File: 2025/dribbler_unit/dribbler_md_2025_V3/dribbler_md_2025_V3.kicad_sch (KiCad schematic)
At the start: 114 parts, among them J2 Conn_01x04_Pin, J3 Conn_01x02_Pin, J4 Conn_01x07_Pin, J5 Conn_01x03_Pin, J6 Conn_01x02_Pin, J7 Conn_01x02_Pin, J8 Conn_01x02_Socket, SW2 SW_MEC_5E, SW4 SW_MEC_5E, U1 MAX3051, U2 STS8DN3LLH5, U3 STS8DN3LLH5, U4 DRV8701, U5 STM32F446RETx, Y1 Crystal_GND2

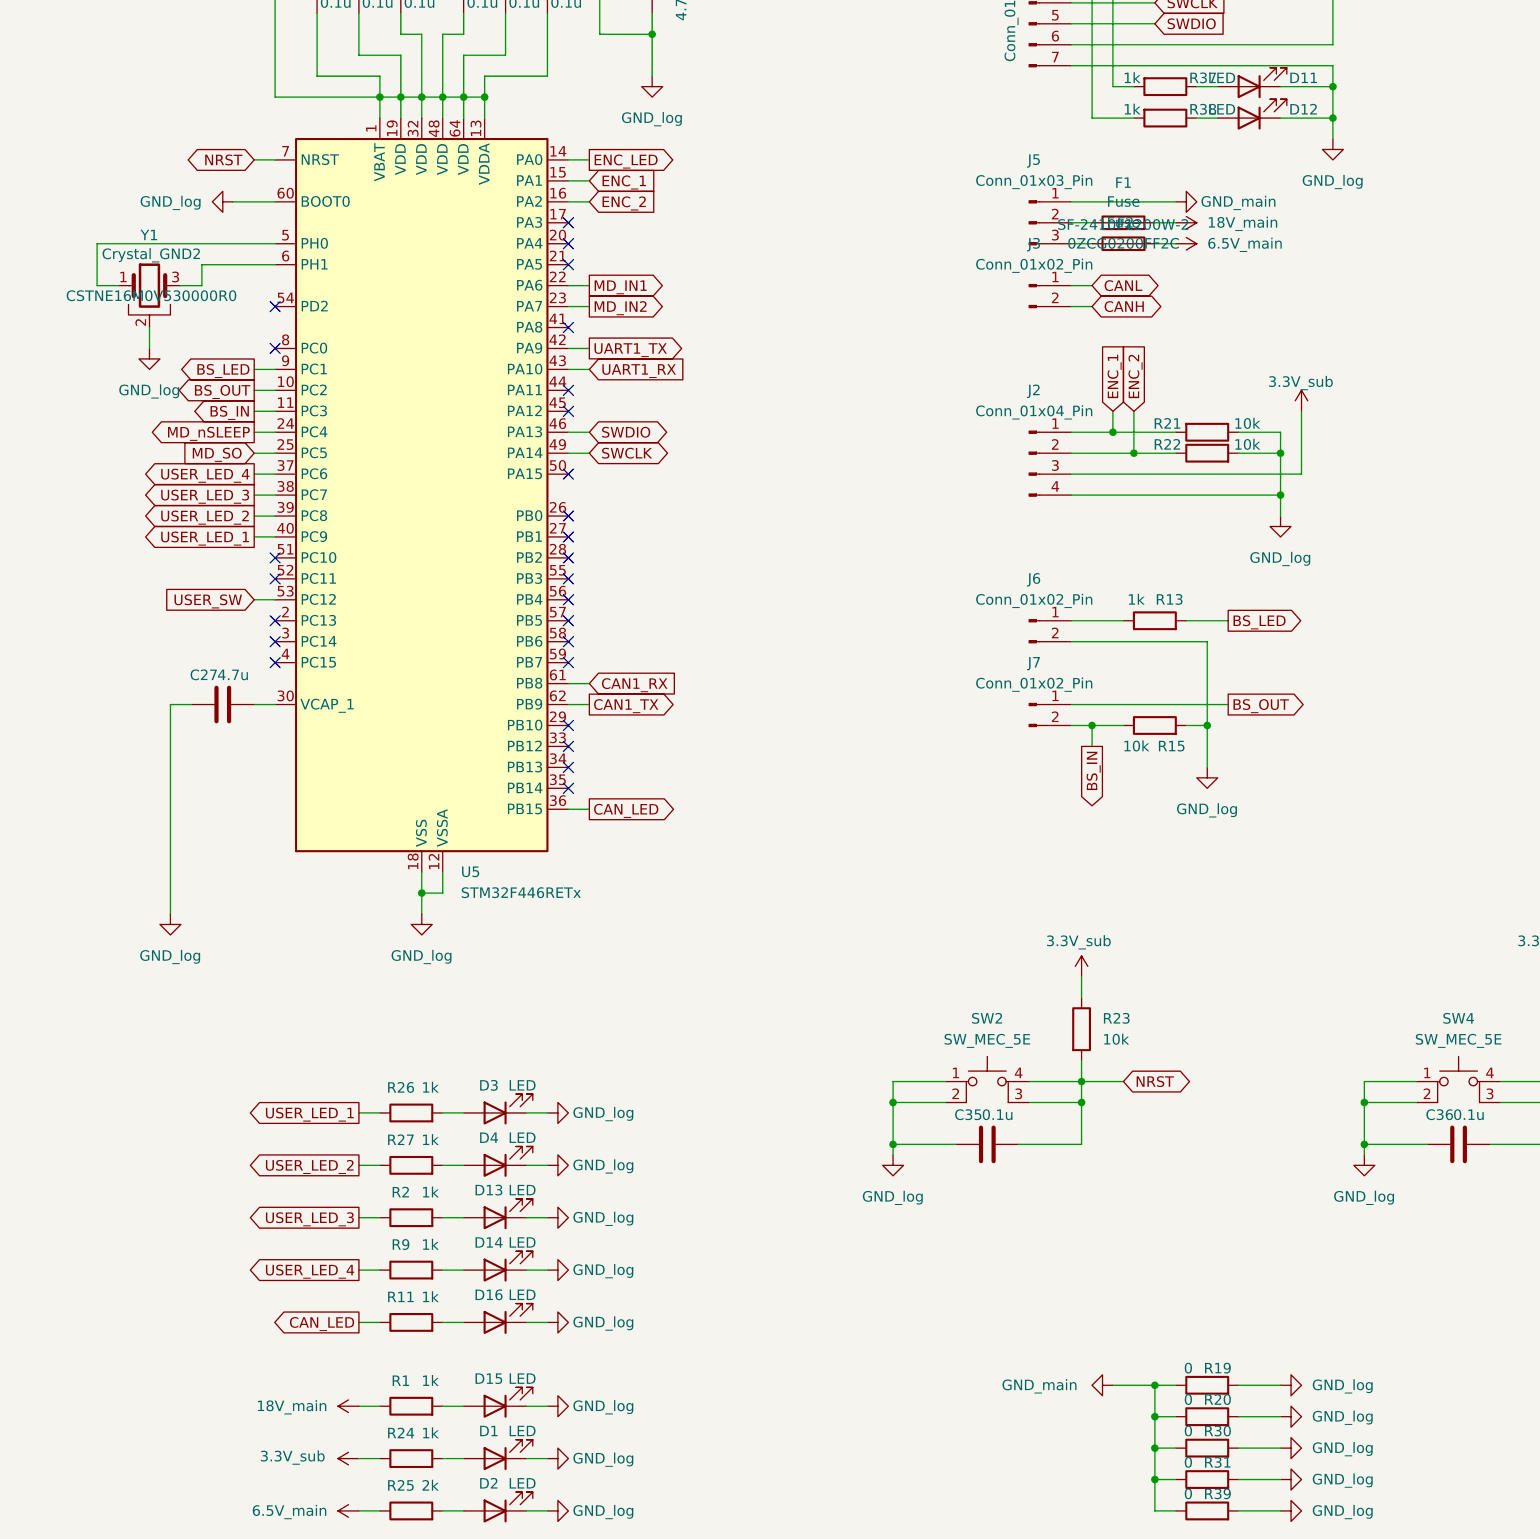
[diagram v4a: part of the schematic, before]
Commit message: stm周りを配線
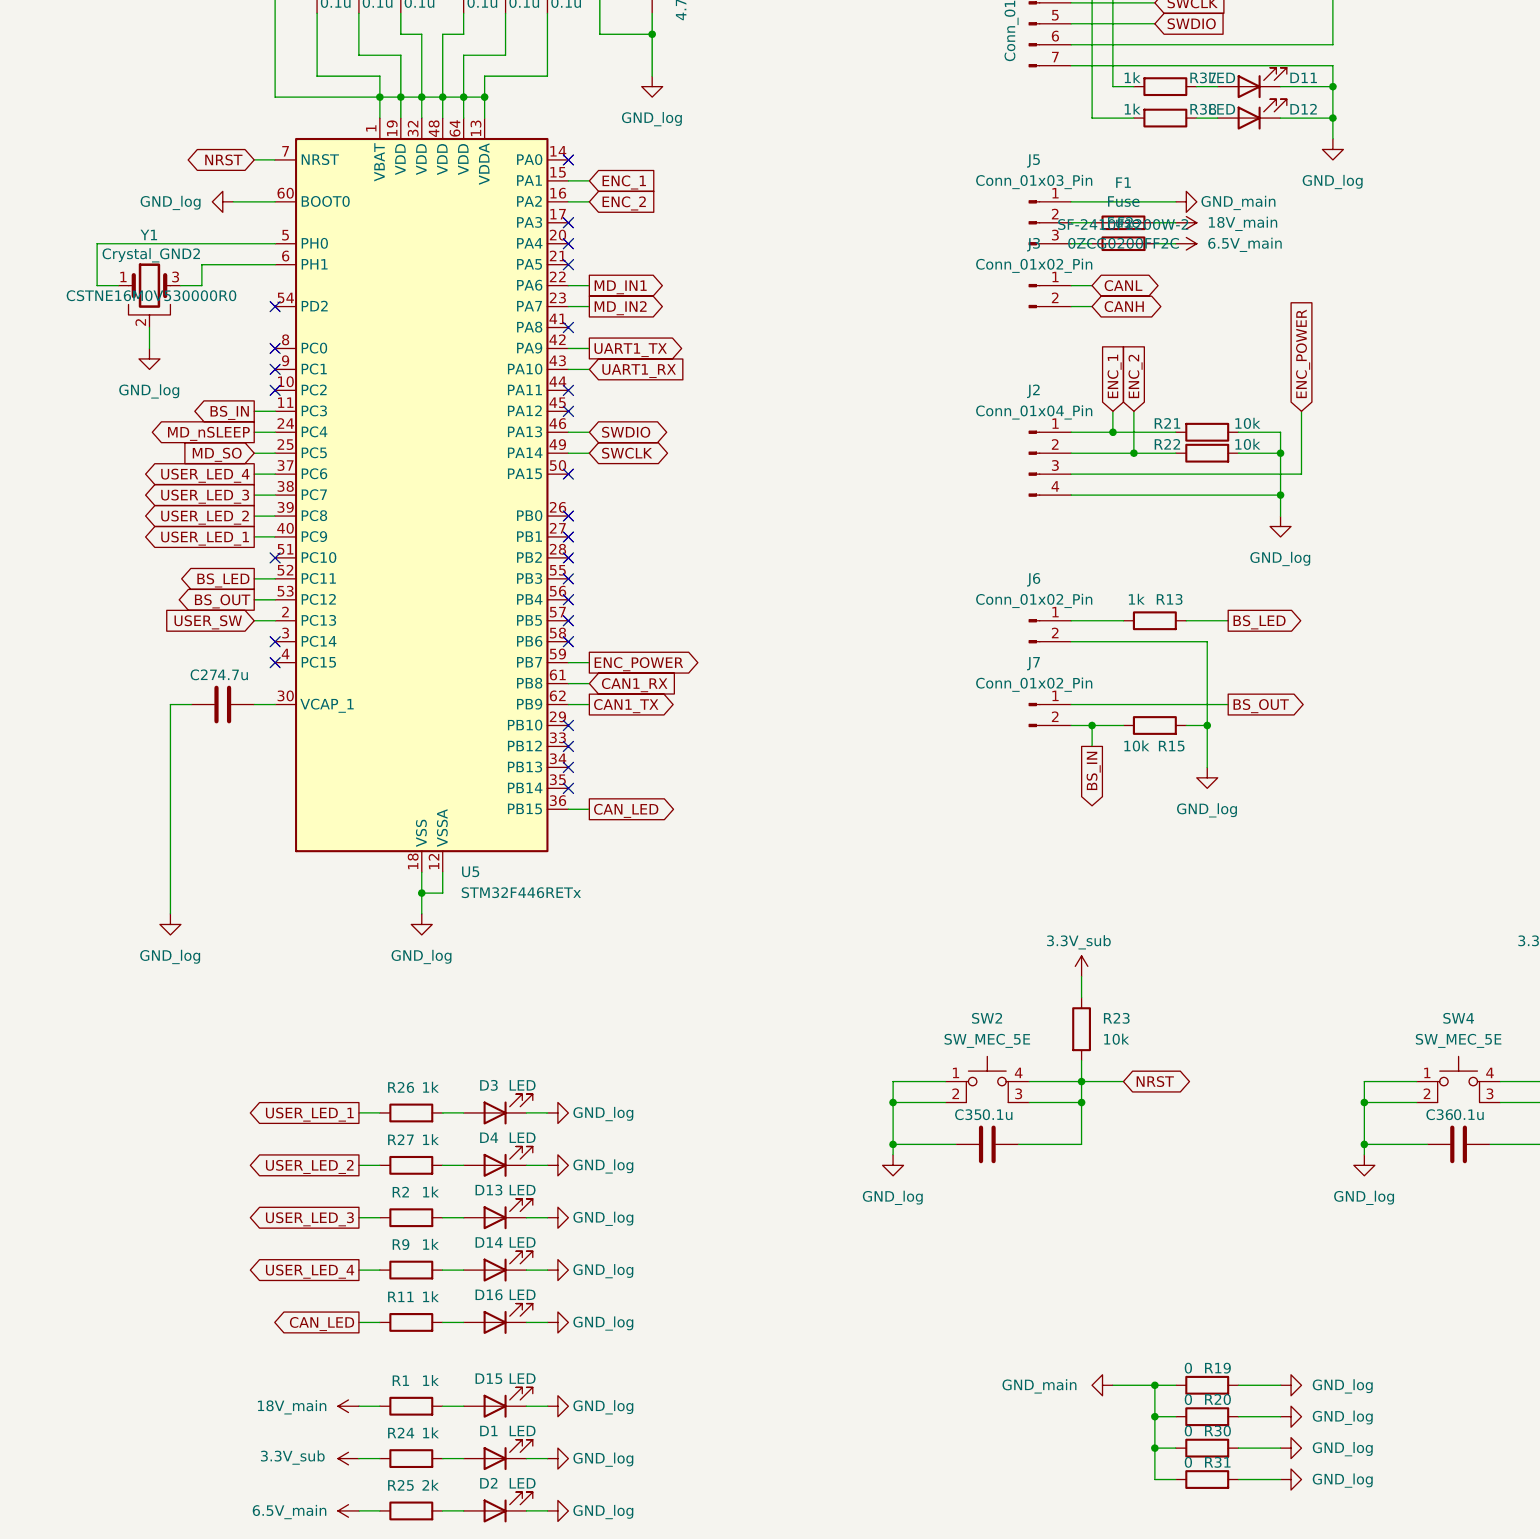
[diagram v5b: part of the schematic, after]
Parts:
- removed R39: 0, Resistor_SMD:R_0603_1608Metric_Pad0.98x0.95mm_HandSolder, symbol Device:R
- R11, R2, R26, R27, R9: footprint Resistor_SMD:R_0603_1608Metric_Pad0.98x0.95mm_HandSolder -> Resistor_SMD:R_0402_1005Metric_Pad0.72x0.64mm_HandSolder
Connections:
- net 3.3V_sub: no longer J2.3 (Pin_3)
- net BS_LED: now also U5.52 (PC11); no longer U5.9 (PC1)
- net BS_OUT: now also U5.53 (PC12); no longer U5.10 (PC2)
- net USER_SW: now also U5.2 (PC13); no longer U5.53 (PC12)
- net ENC_POWER: now reaches U5.59 (PB7)
- net ENC_POWER: now also J2.3 (Pin_3)
- net ENC_LED: no longer names the net of U5.14 (PA0)

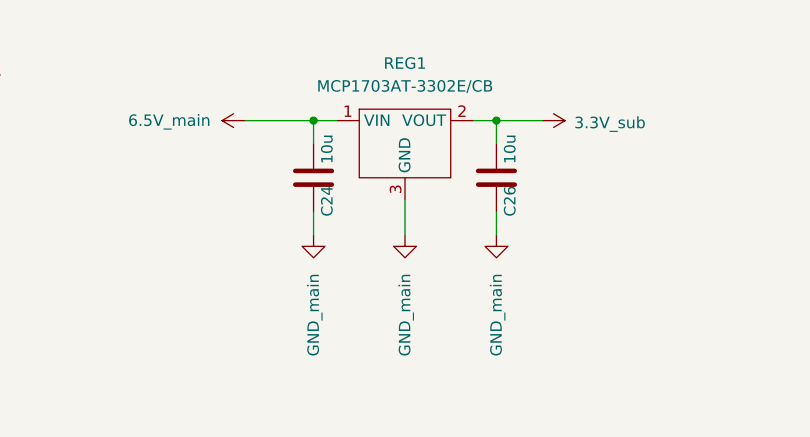
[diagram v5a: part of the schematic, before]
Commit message: 配線完了（ビア打ちは未完了）
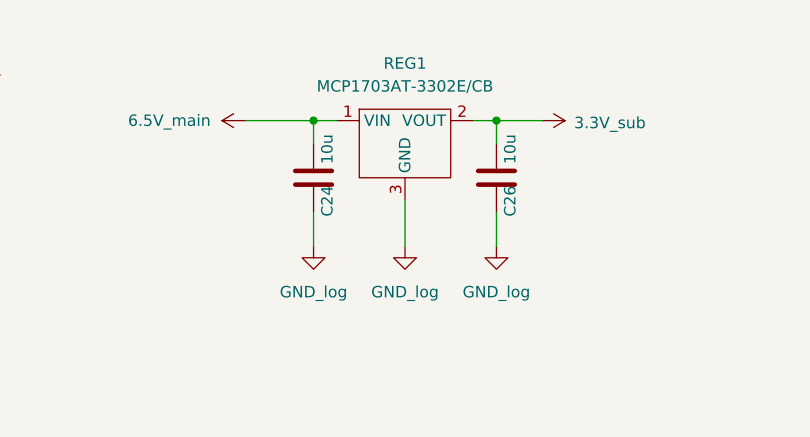
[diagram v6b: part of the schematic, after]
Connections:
- net GND_log: now also C24.2, C26.2, REG1.3 (GND)
- net GND_main: no longer C24.2, C26.2, REG1.3 (GND)
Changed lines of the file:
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@@
 	(wire
 		(pts
-			(xy 149.86 201.93) (xy 149.86 204.47)
-		)
-		(stroke
-			(width 0)
-			(type default)
-		)
-	)
-	(wire
-		(pts
 			(xy 81.28 196.85) (xy 86.36 196.85)
 		)
@@
 	(wire
 		(pts
+			(xy 129.54 201.93) (xy 129.54 205.74)
+		)
+		(stroke
+			(width 0)
+			(type default)
+		)
+	)
+	(wire
+		(pts
 			(xy 92.71 134.62) (xy 100.33 134.62)
 		)
@@
 	(wire
 		(pts
-			(xy 129.54 201.93) (xy 129.54 204.47)
+			(xy 149.86 201.93) (xy 149.86 205.74)
 		)
 		(stroke
@@
 	(wire
 		(pts
+			(xy 139.7 200.66) (xy 139.7 205.74)
+		)
+		(stroke
+			(width 0)
+			(type default)
+		)
+	)
+	(wire
+		(pts
 			(xy 304.8 33.02) (xy 304.8 54.61)
 		)
@@
 	(wire
 		(pts
-			(xy 139.7 200.66) (xy 139.7 204.47)
-		)
-		(stroke
-			(width 0)
-			(type default)
-		)
-	)
-	(wire
-		(pts
 			(xy 302.26 74.93) (xy 304.8 74.93)
 		)
@@
 	)
 	(symbol
+		(lib_id "power:GND")
+		(at 149.86 205.74 0)
+		(unit 1)
+		(exclude_from_sim no)
+		(in_bom yes)
+		(on_board yes)
+		(dnp no)
+		(fields_autoplaced yes)
+		(property "Reference" "#PWR013"
+			(at 149.86 212.09 0)
+			(effects
+				(font
+					(size 1.27 1.27)
+				)
+				(hide yes)
+			)
+		)
+		(property "Value" "GND_log"
+			(at 149.86 210.82 0)
+			(effects
+				(font
+					(size 1.27 1.27)
+				)
+			)
+		)
+		(property "Footprint" ""
+			(at 149.86 205.74 0)
+			(effects
+				(font
+					(size 1.27 1.27)
+				)
+				(hide yes)
+			)
+		)
+		(property "Datasheet" ""
+			(at 149.86 205.74 0)
+			(effects
+				(font
+					(size 1.27 1.27)
+				)
+				(hide yes)
+			)
+		)
+		(property "Description" "Power symbol creates a global label with name \"GND\" , ground"
+			(at 149.86 205.74 0)
+			(effects
+				(font
+					(size 1.27 1.27)
+				)
+				(hide yes)
+			)
+		)
+		(pin "1"
+		)
+		(instances
+			(project "dribbler_md_2025_V3"
+				(path "/fb031fd6-d0d1-41bb-b086-03f1e4d4d794"
+					(reference "#PWR013")
+					(unit 1)
+				)
+			)
+		)
+	)
+	(symbol
 		(lib_id "Device:C")
 		(at 57.15 68.58 0)
@@
 	)
 	(symbol
-		(lib_id "power:GND")
-		(at 139.7 204.47 0)
-		(unit 1)
-		(exclude_from_sim no)
-		(in_bom yes)
-		(on_board yes)
-		(dnp no)
-		(property "Reference" "#PWR015"
-			(at 139.7 210.82 0)
-			(effects
-				(font
-					(size 1.27 1.27)
-				)
-				(hide yes)
-			)
-		)
-		(property "Value" "GND_main"
-			(at 139.7 213.36 90)
-			(effects
-				(font
-					(size 1.27 1.27)
-				)
-			)
-		)
-		(property "Footprint" ""
-			(at 139.7 204.47 0)
-			(effects
-				(font
-					(size 1.27 1.27)
-				)
-				(hide yes)
-			)
-		)
-		(property "Datasheet" ""
-			(at 139.7 204.47 0)
-			(effects
-				(font
-					(size 1.27 1.27)
-				)
-				(hide yes)
-			)
-		)
-		(property "Description" "Power symbol creates a global label with name \"GND\" , ground"
-			(at 139.7 204.47 0)
-			(effects
-				(font
-					(size 1.27 1.27)
-				)
-				(hide yes)
-			)
-		)
-		(pin "1"
-		)
-		(instances
-			(project "dribbler_md_2025_V3"
-				(path "/fb031fd6-d0d1-41bb-b086-03f1e4d4d794"
-					(reference "#PWR015")
-					(unit 1)
-				)
-			)
-		)
-	)
-	(symbol
 		(lib_id "Device:Fuse")
 		(at 308.61 69.85 90)
@@
 	(symbol
 		(lib_id "power:GND")
-		(at 129.54 204.47 0)
-		(unit 1)
-		(exclude_from_sim no)
-		(in_bom yes)
-		(on_board yes)
-		(dnp no)
-		(property "Reference" "#PWR013"
-			(at 129.54 210.82 0)
-			(effects
-				(font
-					(size 1.27 1.27)
-				)
-				(hide yes)
-			)
-		)
-		(property "Value" "GND_main"
-			(at 129.54 213.36 90)
-			(effects
-				(font
-					(size 1.27 1.27)
-				)
-			)
-		)
-		(property "Footprint" ""
-			(at 129.54 204.47 0)
-			(effects
-				(font
-					(size 1.27 1.27)
-				)
-				(hide yes)
-			)
-		)
-		(property "Datasheet" ""
-			(at 129.54 204.47 0)
-			(effects
-				(font
-					(size 1.27 1.27)
-				)
-				(hide yes)
-			)
-		)
-		(property "Description" "Power symbol creates a global label with name \"GND\" , ground"
-			(at 129.54 204.47 0)
-			(effects
-				(font
-					(size 1.27 1.27)
-				)
-				(hide yes)
-			)
-		)
-		(pin "1"
-		)
-		(instances
-			(project "dribbler_md_2025_V3"
-				(path "/fb031fd6-d0d1-41bb-b086-03f1e4d4d794"
-					(reference "#PWR013")
-					(unit 1)
-				)
-			)
-		)
-	)
-	(symbol
-		(lib_id "power:GND")
 		(at 160.02 77.47 0)
 		(unit 1)
@@
 	(symbol
 		(lib_id "power:GND")
-		(at 149.86 204.47 0)
+		(at 139.7 205.74 0)
 		(unit 1)
 		(exclude_from_sim no)
@@
 		(on_board yes)
 		(dnp no)
-		(property "Reference" "#PWR017"
-			(at 149.86 210.82 0)
+		(fields_autoplaced yes)
+		(property "Reference" "#PWR015"
+			(at 139.7 212.09 0)
 			(effects
 				(font
@@
 			)
 		)
-		(property "Value" "GND_main"
-			(at 149.86 213.36 90)
+		(property "Value" "GND_log"
+			(at 139.7 210.82 0)
 			(effects
 				(font
@@
 		)
 		(property "Footprint" ""
-			(at 149.86 204.47 0)
+			(at 139.7 205.74 0)
 			(effects
 				(font
@@
 		)
 		(property "Datasheet" ""
-			(at 149.86 204.47 0)
+			(at 139.7 205.74 0)
 			(effects
 				(font
@@
 		)
 		(property "Description" "Power symbol creates a global label with name \"GND\" , ground"
-			(at 149.86 204.47 0)
+			(at 139.7 205.74 0)
 			(effects
 				(font
@@
 			(project "dribbler_md_2025_V3"
 				(path "/fb031fd6-d0d1-41bb-b086-03f1e4d4d794"
-					(reference "#PWR017")
+					(reference "#PWR015")
 					(unit 1)
 				)
@@
 					(unit 1)
 				)
+			)
+		)
+	)
+	(symbol
+		(lib_id "power:GND")
+		(at 129.54 205.74 0)
+		(unit 1)
+		(exclude_from_sim no)
+		(in_bom yes)
+		(on_board yes)
+		(dnp no)
+		(fields_autoplaced yes)
+		(property "Reference" "#PWR017"
+			(at 129.54 212.09 0)
+			(effects
+				(font
+					(size 1.27 1.27)
+				)
+				(hide yes)
+			)
+		)
+		(property "Value" "GND_log"
+			(at 129.54 210.82 0)
+			(effects
+				(font
+					(size 1.27 1.27)
+				)
+			)
+		)
+		(property "Footprint" ""
+			(at 129.54 205.74 0)
+			(effects
+				(font
+					(size 1.27 1.27)
+				)
+				(hide yes)
+			)
+		)
+		(property "Datasheet" ""
+			(at 129.54 205.74 0)
+			(effects
+				(font
+					(size 1.27 1.27)
+				)
+				(hide yes)
+			)
+		)
+		(property "Description" "Power symbol creates a global label with name \"GND\" , ground"
+			(at 129.54 205.74 0)
+			(effects
+				(font
+					(size 1.27 1.27)
+				)
+				(hide yes)
+			)
+		)
+		(pin "1"
+		)
+		(instances
+			(project "dribbler_md_2025_V3"
+				(path "/fb031fd6-d0d1-41bb-b086-03f1e4d4d794"
+					(reference "#PWR017")
+					(unit 1)
+				)

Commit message: ピン配置変更
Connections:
- net MD_IN1: now also U5.27 (PB1); no longer U5.22 (PA6)
- net MD_IN2: now also U5.26 (PB0); no longer U5.23 (PA7)
- net MD_SO: now also U5.22 (PA6); no longer U5.25 (PC5)
- net MD_nSLEEP: now also U5.23 (PA7); no longer U5.24 (PC4)
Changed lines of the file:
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@@
 	)
 	(no_connect
-		(at 241.3 102.87)
+		(at 241.3 130.81)
 	)
 	(no_connect
-		(at 241.3 130.81)
+		(at 205.74 95.25)
 	)
 	(no_connect
@@
 	)
 	(no_connect
-		(at 241.3 105.41)
-	)
-	(no_connect
 		(at 241.3 115.57)
 	)
@@
 	)
 	(no_connect
+		(at 205.74 92.71)
+	)
+	(no_connect
 		(at 205.74 87.63)
 	)
@@
 	(wire
 		(pts
-			(xy 203.2 95.25) (xy 205.74 95.25)
-		)
-		(stroke
-			(width 0)
-			(type default)
-		)
-	)
-	(wire
-		(pts
 			(xy 36.83 62.23) (xy 41.91 62.23)
 		)
@@
 	(wire
 		(pts
+			(xy 241.3 105.41) (xy 243.84 105.41)
+		)
+		(stroke
+			(width 0)
+			(type default)
+		)
+	)
+	(wire
+		(pts
 			(xy 110.49 57.15) (xy 138.43 57.15)
 		)
@@
 	(wire
 		(pts
+			(xy 241.3 74.93) (xy 243.84 74.93)
+		)
+		(stroke
+			(width 0)
+			(type default)
+		)
+	)
+	(wire
+		(pts
 			(xy 303.53 158.75) (xy 303.53 161.29)
 		)
@@
 	(wire
 		(pts
-			(xy 241.3 77.47) (xy 243.84 77.47)
-		)
-		(stroke
-			(width 0)
-			(type default)
-		)
-	)
-	(wire
-		(pts
 			(xy 129.54 194.31) (xy 129.54 191.77)
 		)
@@
 	(wire
 		(pts
+			(xy 241.3 102.87) (xy 243.84 102.87)
+		)
+		(stroke
+			(width 0)
+			(type default)
+		)
+	)
+	(wire
+		(pts
 			(xy 218.44 52.07) (xy 220.98 52.07)
 		)
@@
 	(wire
 		(pts
-			(xy 203.2 92.71) (xy 205.74 92.71)
-		)
-		(stroke
-			(width 0)
-			(type default)
-		)
-	)
-	(wire
-		(pts
 			(xy 31.75 74.93) (xy 36.83 74.93)
 		)
@@
 	(wire
 		(pts
+			(xy 241.3 77.47) (xy 243.84 77.47)
+		)
+		(stroke
+			(width 0)
+			(type default)
+		)
+	)
+	(wire
+		(pts
 			(xy 15.24 36.83) (xy 15.24 38.1)
 		)
@@
 	(wire
 		(pts
-			(xy 241.3 74.93) (xy 243.84 74.93)
-		)
-		(stroke
-			(width 0)
-			(type default)
-		)
-	)
-	(wire
-		(pts
 			(xy 302.26 69.85) (xy 304.8 69.85)
 		)
@@
 	(global_label "MD_SO"
 		(shape input)
-		(at 203.2 95.25 180)
+		(at 243.84 74.93 0)
 		(fields_autoplaced yes)
 		(effects
@@
 				(size 1.27 1.27)
 			)
-			(justify right)
+			(justify left)
 		)
 		(property "Intersheetrefs" "${INTERSHEET_REFS}"
-			(at 193.9858 95.25 0)
+			(at 253.0542 74.93 0)
 			(effects
 				(font
 					(size 1.27 1.27)
 				)
-				(justify right)
+				(justify left)
 				(hide yes)
 			)
@@
 	(global_label "MD_nSLEEP"
 		(shape output)
-		(at 203.2 92.71 180)
+		(at 243.84 77.47 0)
 		(fields_autoplaced yes)
 		(effects
@@
 				(size 1.27 1.27)
 			)
-			(justify right)
+			(justify left)
 		)
 		(property "Intersheetrefs" "${INTERSHEET_REFS}"
-			(at 189.5712 92.71 0)
+			(at 257.4688 77.47 0)
 			(effects
 				(font
 					(size 1.27 1.27)
 				)
-				(justify right)
+				(justify left)
 				(hide yes)
 			)
@@
 	(global_label "MD_IN2"
 		(shape output)
-		(at 243.84 77.47 0)
+		(at 243.84 102.87 0)
 		(fields_autoplaced yes)
 		(effects
@@
 		)
 		(property "Intersheetrefs" "${INTERSHEET_REFS}"
-			(at 253.659 77.47 0)
+			(at 253.659 102.87 0)
 			(effects
 				(font
@@
 	(global_label "MD_IN1"
 		(shape output)
-		(at 243.84 74.93 0)
+		(at 243.84 105.41 0)
 		(fields_autoplaced yes)
 		(effects
@@
 		)
 		(property "Intersheetrefs" "${INTERSHEET_REFS}"
-			(at 253.659 74.93 0)
+			(at 253.659 105.41 0)
 			(effects
 				(font

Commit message: シルク追加&stepファイル出力
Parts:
- J3: footprint Connector_Molex:Molex_SPOX_5268-02A_1x02_P2.50mm_Horizontal -> Connector_JST:JST_PH_S2B-PH-K_1x02_P2.00mm_Horizontal
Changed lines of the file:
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@@
 			)
 		)
-		(property "Footprint" "Connector_Molex:Molex_SPOX_5268-02A_1x02_P2.50mm_Horizontal"
+		(property "Footprint" "Connector_JST:JST_PH_S2B-PH-K_1x02_P2.00mm_Horizontal"
 			(at 297.18 74.93 0)
 			(effects
